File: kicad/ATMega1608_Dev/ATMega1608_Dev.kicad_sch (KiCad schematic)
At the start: 36 parts, among them J1 Alt Power, J2 USB_B_Micro, J3 Comm, J4 GPIO1, J5 GPIO2, J6 Power OUT, U1 TC1262-33, U2 FT232RQ, U3 ATMega1608_32

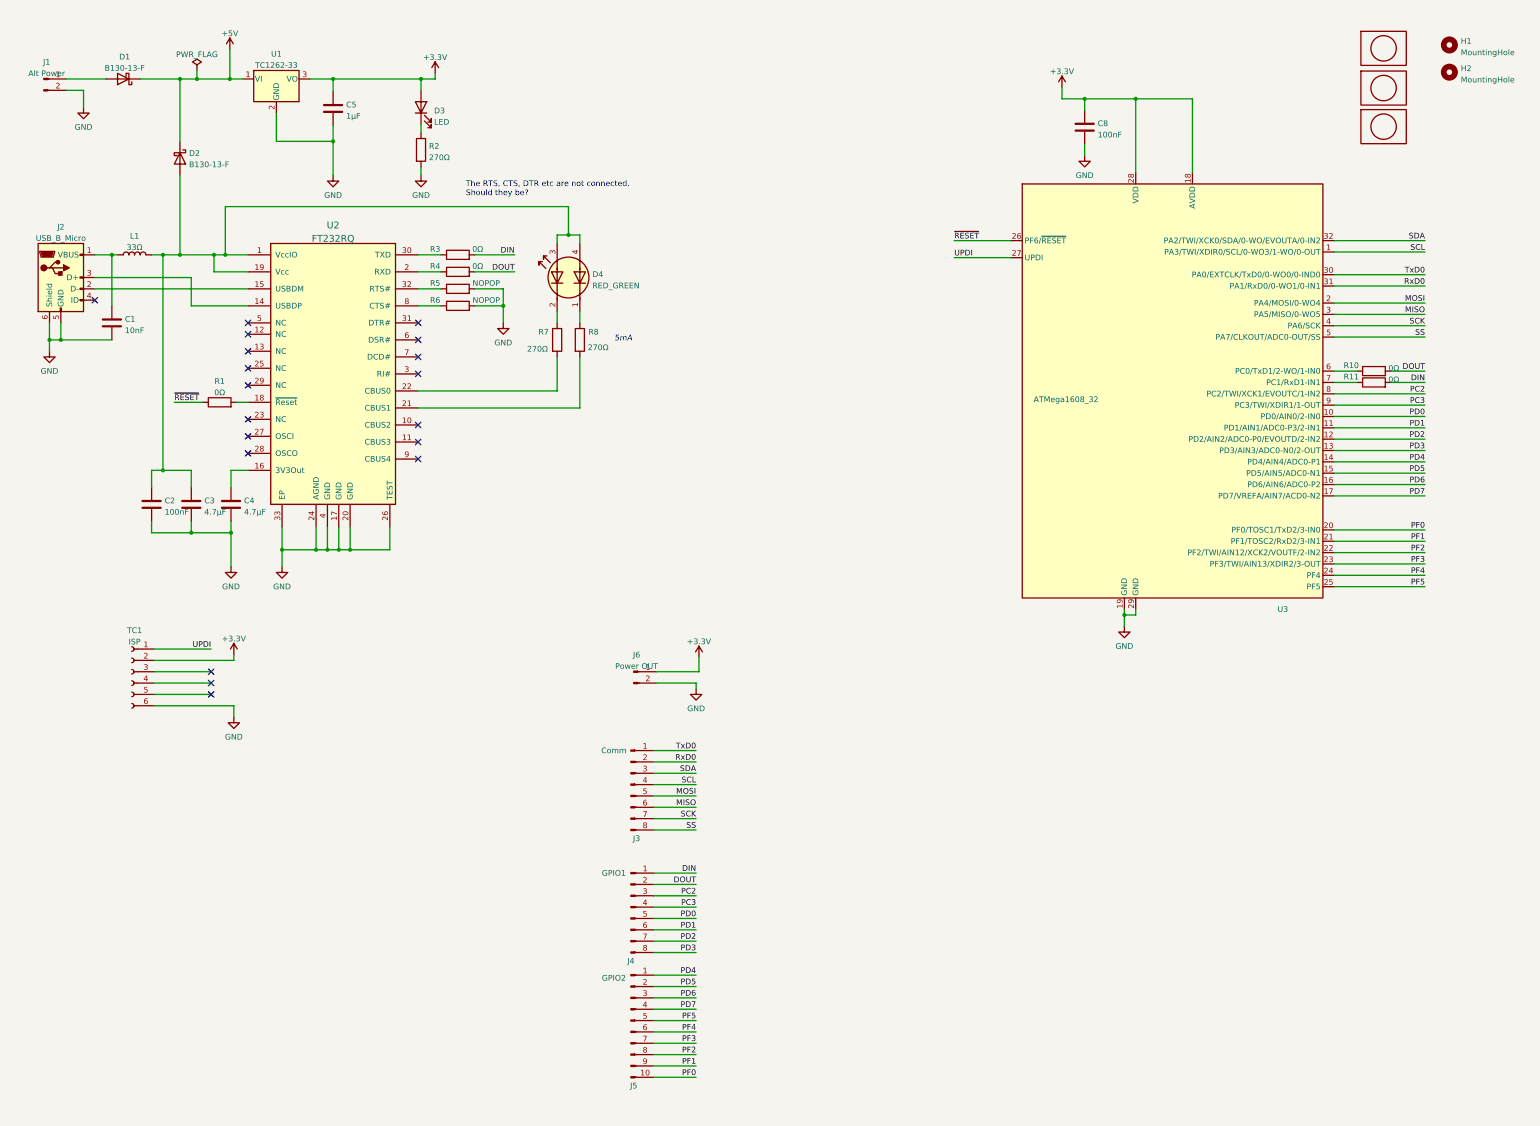
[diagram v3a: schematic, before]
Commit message: Fixes some labeling issues
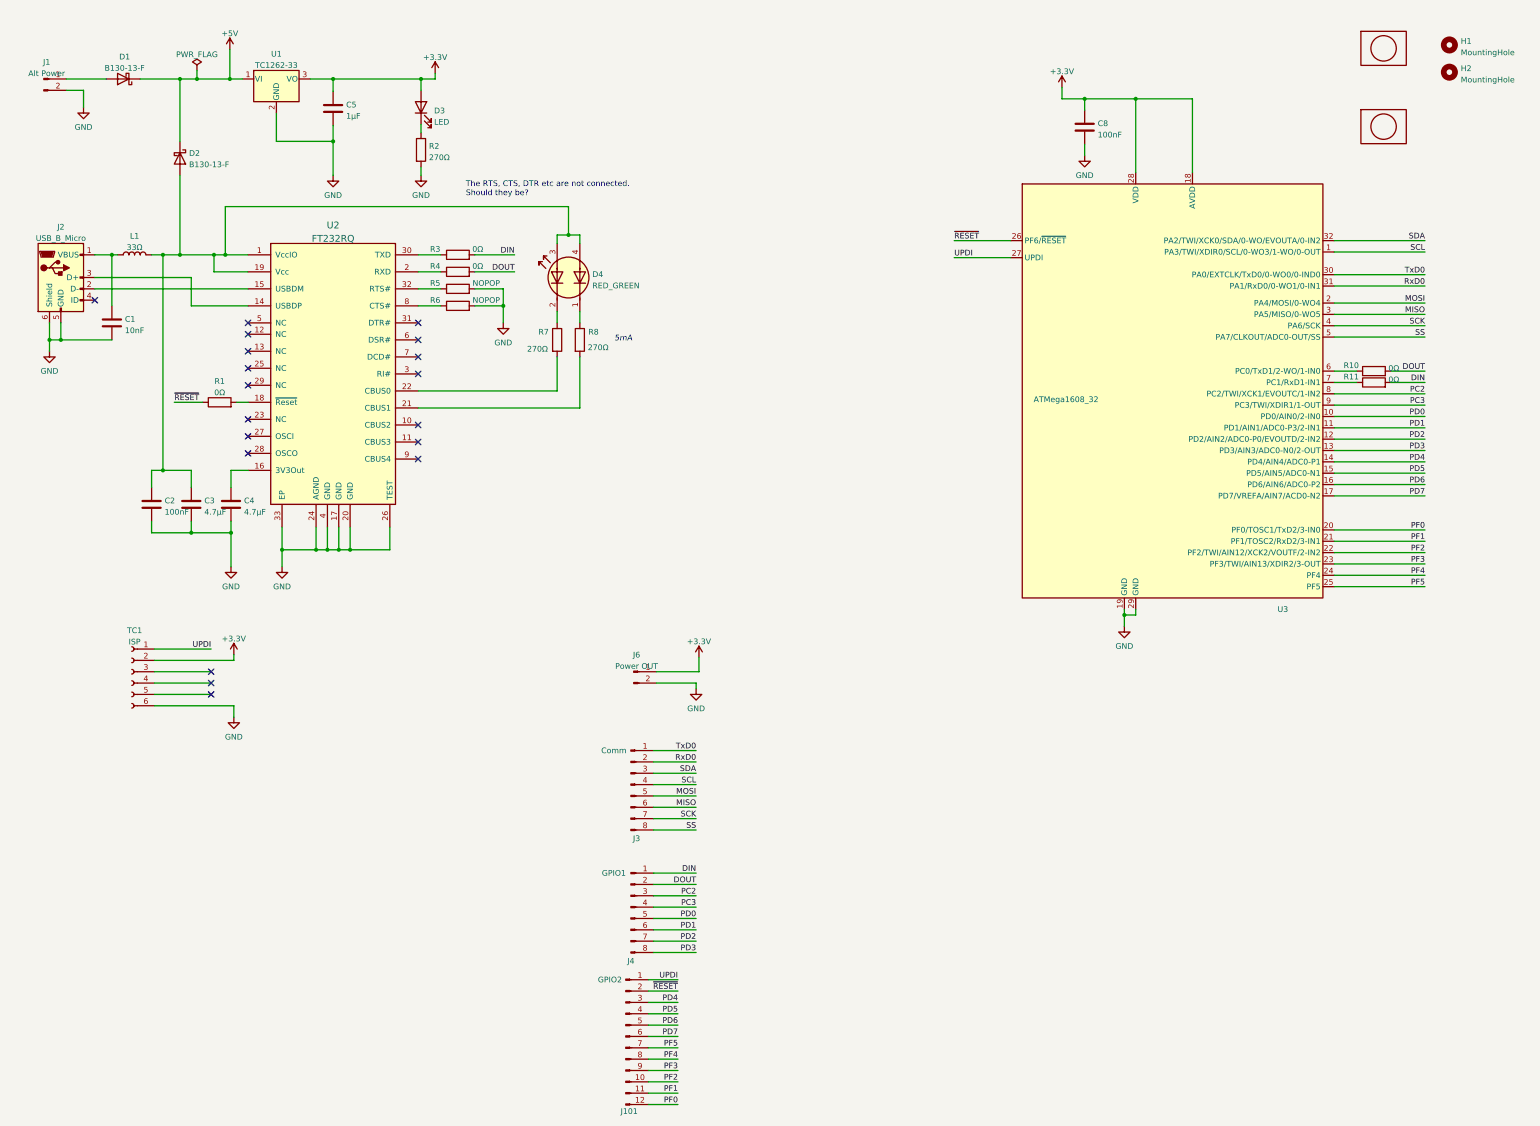
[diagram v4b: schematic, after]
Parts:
- removed J5: GPIO2, Connector_PinHeader_2.54mm:PinHeader_1x10_P2.54mm_Vertical, symbol Connector:Conn_01x10_Male
- removed LG2: logo, mech:MyBasic_rounded_50_1, symbol mech:logo
- added J101: GPIO2, Connector_PinHeader_2.54mm:PinHeader_1x12_P2.54mm_Vertical, symbol Connector:Conn_01x12_Male
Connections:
- net PD4: now also J101.3 (Pin_3)
- net PD5: now also J101.4 (Pin_4)
- net PD6: now also J101.5 (Pin_5)
- net PD7: now also J101.6 (Pin_6)
- net PF0: now also J101.12 (Pin_12)
- net PF1: now also J101.11 (Pin_11)
- net PF2: now also J101.10 (Pin_10)
- net PF3: now also J101.9 (Pin_9)
- net PF4: now also J101.8 (Pin_8)
- net PF5: now also J101.7 (Pin_7)
- net UPDI: now also J101.1 (Pin_1)
- net ~{RESET}: now also J101.2 (Pin_2)

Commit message: Moved the USART_Troubleshooting changes to main
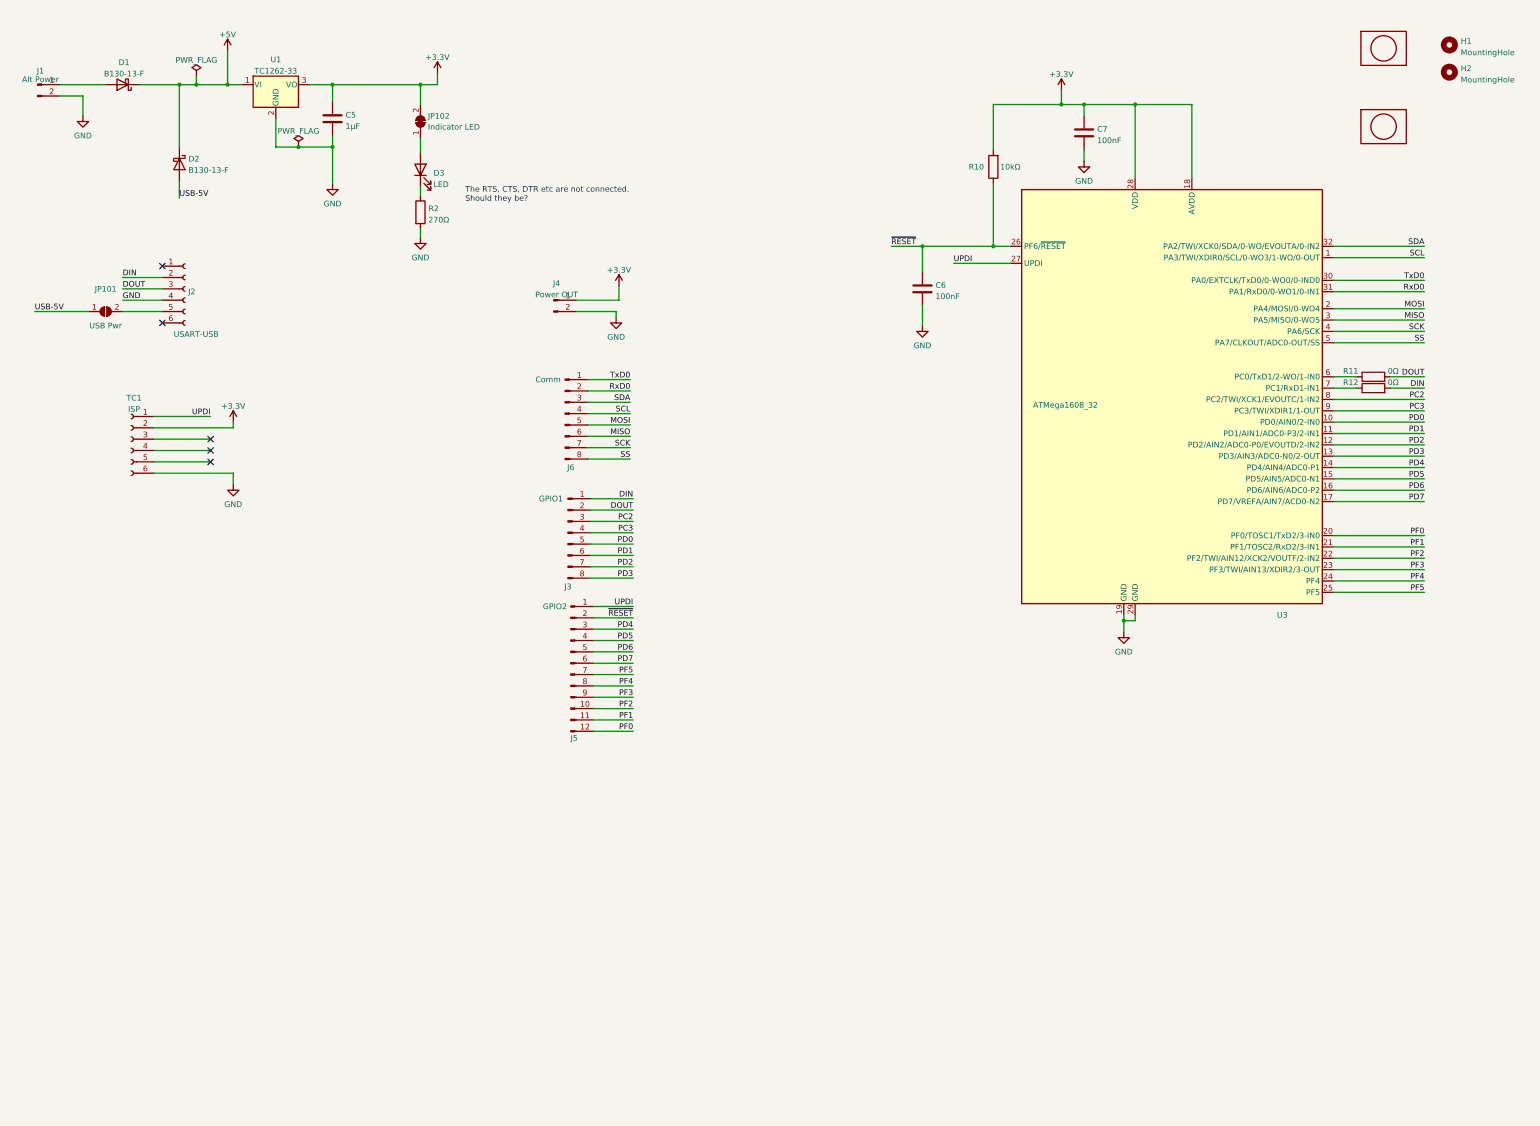
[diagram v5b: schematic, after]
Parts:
- removed C1: 10nF, Capacitor_SMD:C_0805_2012Metric, symbol Device:C
- removed C2: 100nF, Capacitor_SMD:C_0805_2012Metric, symbol Device:C
- removed C3, C4: 4.7μF, Capacitor_SMD:C_0805_2012Metric, symbol Device:C
- removed D4: RED_GREEN, atmega1608_footprints:LED_KKAA_15-22SURSYGC, symbol atmega1608_dev:LED_Dual_KKAA
- removed J1: Alt Power, Connector_PinHeader_2.54mm:PinHeader_1x02_P2.54mm_Vertical, symbol Connector:Conn_01x02_Male
- removed J2: USB_B_Micro, Connector_USB:USB_Micro-B_Amphenol_10103594-0001LF_Horizontal, symbol Connector:USB_B_Micro
- removed L1: 33Ω, Inductor_SMD:L_1206_3216Metric, symbol Device:L
- removed R1, R3, R4: 0Ω, Resistor_SMD:R_0805_2012Metric, symbol Device:R
- removed R5, R6: NOPOP, Resistor_SMD:R_0805_2012Metric, symbol Device:R
- removed R7, R8: 270Ω, Resistor_SMD:R_0805_2012Metric, symbol Device:R
- removed U2: FT232RQ, Package_DFN_QFN:QFN-32-1EP_5x5mm_P0.5mm_EP3.3x3.3mm_ThermalVias, symbol atmega1608_dev:FT232RQ
- added C6: 100nF, Capacitor_SMD:C_0805_2012Metric, symbol Device:C
- added J1: Alt Power, Connector_PinHeader_2.54mm:PinHeader_1x02_P2.54mm_Vertical, symbol Connector:Conn_01x02_Pin
- added J2: USART-USB, Connector_PinSocket_2.54mm:PinSocket_1x06_P2.54mm_Vertical, symbol Connector:Conn_01x06_Socket
- added JP101: USB Pwr, Connector_PinHeader_2.54mm:PinHeader_1x02_P2.54mm_Vertical, symbol Jumper:SolderJumper_2_Open
- added JP102: Indicator LED, Jumper:SolderJumper-2_P1.3mm_Bridged_RoundedPad1.0x1.5mm, symbol Jumper:SolderJumper_2_Bridged
- added R10: 10kΩ, Resistor_SMD:R_0805_2012Metric, symbol Device:R
- J3: renamed from J4; symbol Connector:Conn_01x08_Male -> Connector:Conn_01x08_Pin
- J4: renamed from J6; symbol Connector:Conn_01x02_Male -> Connector:Conn_01x02_Pin
- J5: renamed from J101; symbol Connector:Conn_01x12_Male -> Connector:Conn_01x12_Pin
- J6: renamed from J3; symbol Connector:Conn_01x08_Male -> Connector:Conn_01x08_Pin
- renumbered C8 to C7, LG3 to LG2, R10 to R11, R11 to R12
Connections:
- net DIN: now also J2.2 (Pin_2)
- net DOUT: now also J2.3 (Pin_3)
- net GND: now also C6.2, J1.2 (Pin_2), J2.4 (Pin_4)
- net ~{RESET}: now also C6.1, R10.1
- net USB-5V: now reaches D2.2 (A)
- net USB-5V: now also JP101.1 (A)
- net at D1.2 (A): now also J1.1 (Pin_1)
- net +3V3 renamed +3.3V
- net +3.3V: now also JP102.2 (B), R10.2; no longer D3.2 (A)
- new net: J2.5 (Pin_5), JP101.2 (B)
- new net: D3.2 (A), JP102.1 (A)
- no-connect marks 19 -> 5
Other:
- note removed: "5mA"
- moved on the sheet: C5, C7, D1, D2, D3, J3, J4, J5, J6, R11, R12, R2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

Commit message: Revision 1.2 - Update to connectors, jumpers and labels
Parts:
- removed J3: GPIO1, Connector_PinHeader_2.54mm:PinHeader_1x08_P2.54mm_Vertical, symbol Connector:Conn_01x08_Pin
- removed J6: Comm, Connector_PinHeader_2.54mm:PinHeader_1x08_P2.54mm_Vertical, symbol Connector:Conn_01x08_Pin
- added J3: GPIO, Connector_PinHeader_2.54mm:PinHeader_1x16_P2.54mm_Vertical, symbol Connector:Conn_01x16_Pin
- added LG3: logo, mech:MyBasic_rounded_50_1, symbol mech:logo
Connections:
- net PF2 is gone; now on net SDA: J5.10 (Pin_10), U3.22 (PF2/TWI/AIN12/XCK2/VOUTF/2-IN2)
- net PF3 is gone; now on net SCL: J5.9 (Pin_9), U3.23 (PF3/TWI/AIN13/XDIR2/3-OUT)
- net DIN: now also J3.9 (Pin_9)
- net DOUT: now also J3.10 (Pin_10)
- net MISO: now also J3.6 (Pin_6)
- net MOSI: now also J3.5 (Pin_5)
- net PC2: now also J3.11 (Pin_11)
- net PC3: now also J3.12 (Pin_12)
- net PD0: now also J3.13 (Pin_13)
- net PD1: now also J3.14 (Pin_14)
- net PD2: now also J3.15 (Pin_15)
- net PD3: now also J3.16 (Pin_16)
- net RxD0: now also J3.2 (Pin_2)
- net SCK: now also J3.7 (Pin_7)
- net SCL: no longer U3.1 (PA3/TWI/XDIR0/SCL/0-WO3/1-WO/0-OUT)
- net SDA: no longer U3.32 (PA2/TWI/XCK0/SDA/0-WO/EVOUTA/0-IN2)
- net SS: now also J3.8 (Pin_8)
- net TxD0: now also J3.1 (Pin_1)
- new net PA2: J3.3 (Pin_3), U3.32 (PA2/TWI/XCK0/SDA/0-WO/EVOUTA/0-IN2)
- new net PA3: J3.4 (Pin_4), U3.1 (PA3/TWI/XDIR0/SCL/0-WO3/1-WO/0-OUT)
